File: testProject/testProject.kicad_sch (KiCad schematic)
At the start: 2 parts

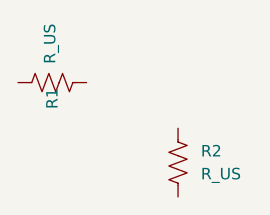
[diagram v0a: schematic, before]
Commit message: Fixed the symbol subsection error
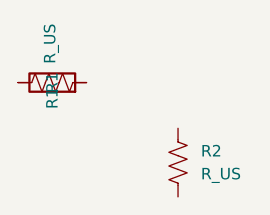
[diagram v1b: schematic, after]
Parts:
- added R1: (no value), symbol Device:R
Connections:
- net at R1.1: now also R1.1
- net at R1.2: now also R1.2
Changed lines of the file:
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@@
 	(generator_version "8.0")
 	(paper "A4")
-	(symbol
+(symbol
+        (lib_id "Device:R")
+        (at 146.05 53.34 90)
+        (unit 1)
+        (exclude_from_sim no)
+        (in_bom yes)
+        (on_board yes)
+        (dnp no)
+        (fields_autoplaced yes)
+        (property "Reference" "R1"
+            (at 146.05 53.34 0)
+            (effects
+                (font
+                    (size 1.27 1.27)
+                )
+            )
+        )
+        (property "Value" ""
+            (at 146.05 53.34 0)
+            (effects
+                (font
+                    (size 1.27 1.27)
+                )
+            )
+        )
+        (property "Footprint" ""
+            (at 146.05 53.34 0)
+            (effects
+                (font
+                    (size 1.27 1.27)
+                )
+                (hide yes)
+            )
+        )
+        (property "Datasheet" "~"
+            (at 146.05 53.34 0)
+            (effects
+                (font
+                    (size 1.27 1.27)
+                )
+                (hide yes)
+            )
+        )
+        (property "Description" "esistor"
+            (at 146.05 53.34 0)
+            (effects
+                (font
+                    (size 1.27 1.27)
+                )
+                (hide yes)
+            )
+        )
+        (instances
+            (project "temp_59526c9f-d2d4-4c47-ba25-9347dc717d36"
+                (path "/59526c9f-d2d4-4c47-ba25-9347dc717d36"
+                    (reference "R1")
+                    (unit 1)
+                )
+            )
+        )
+    )
+ 	(symbol
 		(lib_id "Device:R_US")
 		(at 146.05 53.34 90)

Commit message: The thing is buggy but it works
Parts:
- removed R1, R2: R_US, symbol Device:R_US
- removed R1: (no value), symbol Device:R
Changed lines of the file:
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@@
 	(generator_version "8.0")
 	(paper "A4")
-(symbol
-        (lib_id "Device:R")
-        (at 146.05 53.34 90)
-        (unit 1)
-        (exclude_from_sim no)
-        (in_bom yes)
-        (on_board yes)
-        (dnp no)
-        (fields_autoplaced yes)
-        (property "Reference" "R1"
-            (at 146.05 53.34 0)
-            (effects
-                (font
-                    (size 1.27 1.27)
-                )
-            )
-        )
-        (property "Value" ""
-            (at 146.05 53.34 0)
-            (effects
-                (font
-                    (size 1.27 1.27)
-                )
-            )
-        )
-        (property "Footprint" ""
-            (at 146.05 53.34 0)
-            (effects
-                (font
-                    (size 1.27 1.27)
-                )
-                (hide yes)
-            )
-        )
-        (property "Datasheet" "~"
-            (at 146.05 53.34 0)
-            (effects
-                (font
-                    (size 1.27 1.27)
-                )
-                (hide yes)
-            )
-        )
-        (property "Description" "esistor"
-            (at 146.05 53.34 0)
-            (effects
-                (font
-                    (size 1.27 1.27)
-                )
-                (hide yes)
-            )
-        )
-        (instances
-            (project "temp_59526c9f-d2d4-4c47-ba25-9347dc717d36"
-                (path "/59526c9f-d2d4-4c47-ba25-9347dc717d36"
-                    (reference "R1")
-                    (unit 1)
-                )
-            )
-        )
-    )
- 	(symbol
-		(lib_id "Device:R_US")
-		(at 146.05 53.34 90)
-		(unit 1)
-		(exclude_from_sim no)
-		(in_bom yes)
-		(on_board yes)
-		(dnp no)
-		(property "Reference" "R1"
-			(at 146.05 55.118 0)
-			(effects
-				(font
-					(size 1.27 1.27)
-				)
-			)
-		)
-		(property "Value" "R_US"
-			(at 145.796 49.022 0)
-			(effects
-				(font
-					(size 1.27 1.27)
-				)
-			)
-		)
-		(property "Footprint" ""
-			(at 146.05 53.34 0)
-			(effects
-				(font
-					(size 1.27 1.27)
-				)
-				(hide yes)
-			)
-		)
-		(property "Datasheet" "~"
-			(at 146.05 53.34 0)
-			(effects
-				(font
-					(size 1.27 1.27)
-				)
-				(hide yes)
-			)
-		)
-		(property "Description" "esistor, US symbol"
-			(at 146.05 53.34 0)
-			(effects
-				(font
-					(size 1.27 1.27)
-				)
-				(hide yes)
-			)
-		)
-		(pin "2"
-		)
-		(pin "1"
-		)
-		(instances
-			(project "testProject"
-				(path "/59526c9f-d2d4-4c47-ba25-9347dc717d36"
-					(reference "R1")
-					(unit 1)
-				)
-			)
-		)
-	)
-	(symbol
-		(lib_id "Device:R_US")
-		(at 160.02 62.23 0)
-		(unit 1)
-		(exclude_from_sim no)
-		(in_bom yes)
-		(on_board yes)
-		(dnp no)
-		(fields_autoplaced yes)
-		(property "Reference" "R2"
-			(at 162.56 60.9599 0)
-			(effects
-				(font
-					(size 1.27 1.27)
-				)
-				(justify left)
-			)
-		)
-		(property "Value" "R_US"
-			(at 162.56 63.4999 0)
-			(effects
-				(font
-					(size 1.27 1.27)
-				)
-				(justify left)
-			)
-		)
-		(property "Footprint" ""
-			(at 161.036 62.484 90)
-			(effects
-				(font
-					(size 1.27 1.27)
-				)
-				(hide yes)
-			)
-		)
-		(property "Datasheet" "~"
-			(at 160.02 62.23 0)
-			(effects
-				(font
-					(size 1.27 1.27)
-				)
-				(hide yes)
-			)
-		)
-		(property "Description" "Resistor, US symbol"
-			(at 160.02 62.23 0)
-			(effects
-				(font
-					(size 1.27 1.27)
-				)
-				(hide yes)
-			)
-		)
-		(pin "2"
-		)
-		(pin "1"
-		)
-		(instances
-			(project "testProject"
-				(path "/59526c9f-d2d4-4c47-ba25-9347dc717d36"
-					(reference "R2")
-					(unit 1)
-				)
-			)
-		)
-	)
 	(sheet_instances
 		(path "/"

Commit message: cleaned up notebook
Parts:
- added C1, C2: C, symbol Device:C
- added R1: R, symbol Device:R
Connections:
- new net: C2.1, R1.1
- new net: C1.1, C2.2
- new net: C1.2, R1.2

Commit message: changed config.yaml
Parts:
- removed C1, C2: C, symbol Device:C
- removed R1: R, symbol Device:R

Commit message: Added add_wires in GUI
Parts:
- added BAT1: attery, symbol Device:Battery
- added LED1: ED, symbol Device:LED
- added R1: (no value), symbol Device:R
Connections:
- new net: BAT1.1 (+), R1.2
- new net: BAT1.2 (-), LED1.1 (K), LED1.2 (A), R1.1

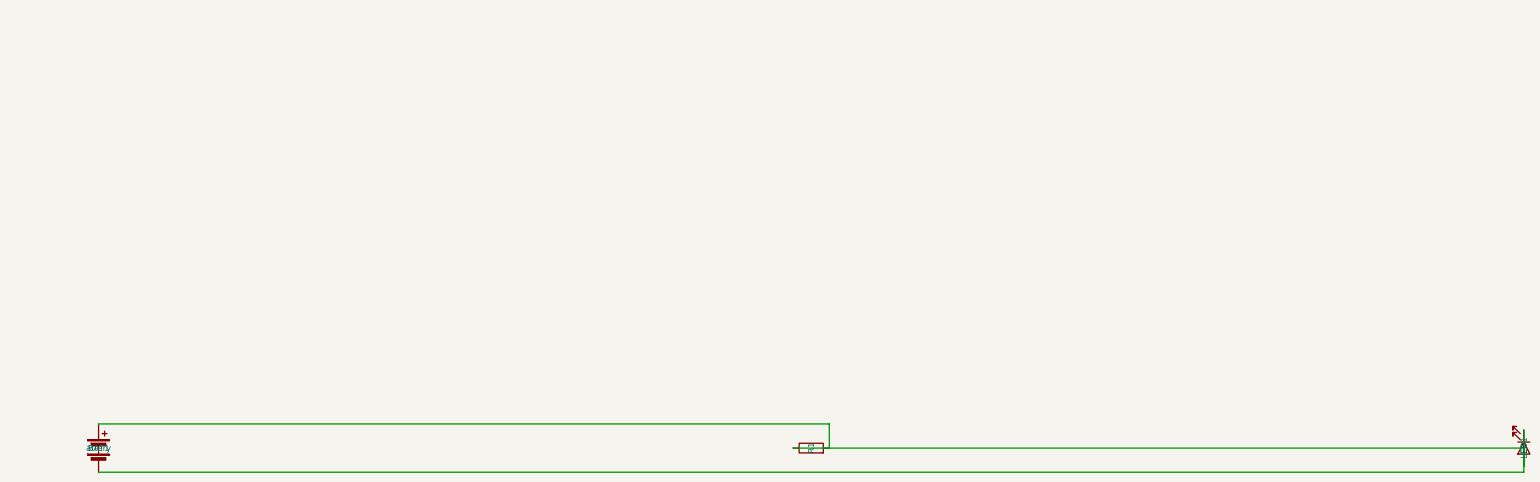
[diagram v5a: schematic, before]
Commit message: still needs error handling for wire functions
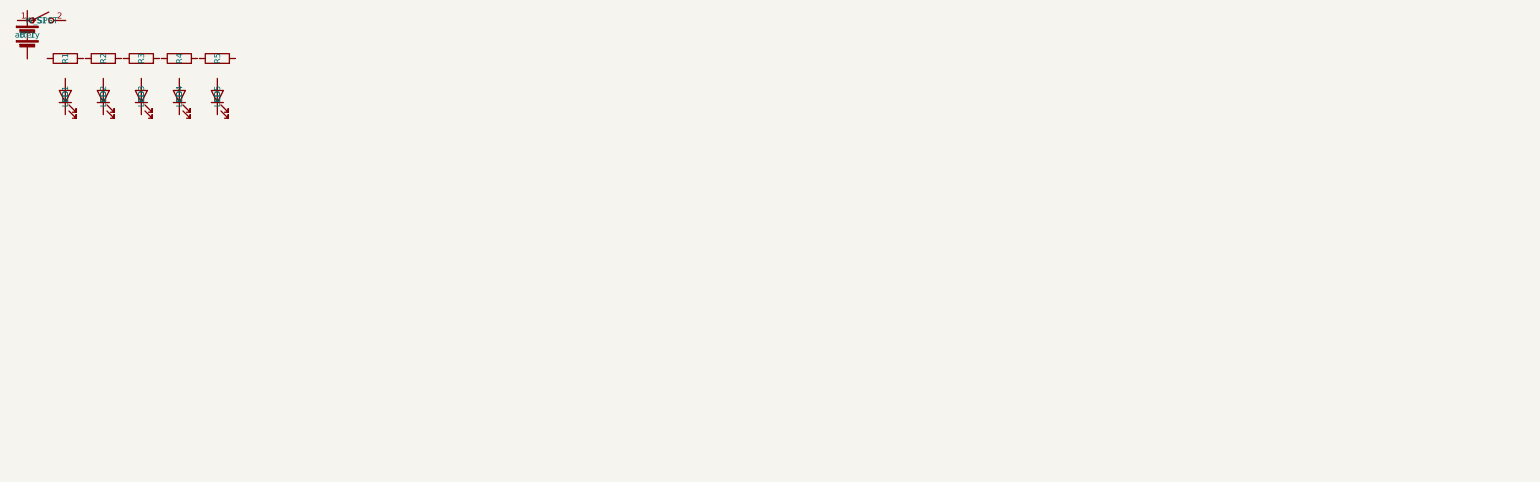
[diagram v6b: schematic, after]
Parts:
- removed BAT1: attery, symbol Device:Battery
- added BT1: attery, symbol Device:Battery
- added LED2, LED3, LED4, LED5: ED, symbol Device:LED
- added R2, R3, R4, R5: (no value), symbol Device:R
- added S1: W_SPST, symbol Switch:SW_SPST
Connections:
- now unconnected: LED1.1 (K), LED1.2 (A), R1.1

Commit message: exit
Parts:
- removed LED1, LED2, LED3, LED4, LED5: ED, symbol Device:LED
- removed R2, R3, R4, R5: (no value), symbol Device:R
- removed S1: W_SPST, symbol Switch:SW_SPST
- added C1: (no value), symbol Device:C
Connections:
- net at BT1.1 (+): now also R1.1
- net at BT1.2 (-): now also C1.2
- net at R1.2: now also C1.1

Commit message: removed unneccessary files, clean up notebook
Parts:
- removed BT1: attery, symbol Device:Battery
- removed C1: (no value), symbol Device:C
- removed R1: (no value), symbol Device:R
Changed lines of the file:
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@@
 	(generator_version "8.0")
 	(paper "A4")
- (wire
-		(pts
-			(xy 42 14.92) (xy 42 16.19)
-		)
-		(stroke
-			(width 0)
-			(type default)
-		)
-	)
- (wire
-		(pts
-			(xy 20 14.92) (xy 42 14.92)
-		)
-		(stroke
-			(width 0)
-			(type default)
-		)
-	)
- (wire
-		(pts
-			(xy 42 23.81) (xy 42 28.19)
-		)
-		(stroke
-			(width 0)
-			(type default)
-		)
-	)
- (wire
-		(pts
-			(xy 20 35.81) (xy 20 25.08)
-		)
-		(stroke
-			(width 0)
-			(type default)
-		)
-	)
- (wire
-		(pts
-			(xy 42 35.81) (xy 20 35.81)
-		)
-		(stroke
-			(width 0)
-			(type default)
-		)
-	)
-(symbol
-        (lib_id "Device:C")
-        (at 42 32 0)
-        (unit 1)
-        (exclude_from_sim no)
-        (in_bom yes)
-        (on_board yes)
-        (dnp no)
-        (fields_autoplaced yes)
-        (property "Reference" "C1"
-            (at 42 32 0)
-            (effects
-                (font
-                    (size 1.27 1.27)
-                )
-            )
-        )
-        (property "Value" ""
-            (at 42 32 0)
-            (effects
-                (font
-                    (size 1.27 1.27)
-                )
-            )
-        )
-        (property "Footprint" ""
-            (at 42 32 0)
-            (effects
-                (font
-                    (size 1.27 1.27)
-                )
-                (hide yes)
-            )
-        )
-        (property "Datasheet" "~"
-            (at 42 32 0)
-            (effects
-                (font
-                    (size 1.27 1.27)
-                )
-                (hide yes)
-            )
-        )
-        (property "Description" "npolarized capacitor"
-            (at 42 32 0)
-            (effects
-                (font
-                    (size 1.27 1.27)
-                )
-                (hide yes)
-            )
-        )
-        (pin "1")
-        (pin "2")
-        (instances
-            (project "temp_dea647a7-e0d8-45e4-9bce-23c7e387cf2b"
-                (path "/dea647a7-e0d8-45e4-9bce-23c7e387cf2b"
-                    (reference "C1")
-                    (unit 1)
-                )
-            )
-        )
-    )
-(symbol
-        (lib_id "Device:R")
-        (at 42 20 0)
-        (unit 1)
-        (exclude_from_sim no)
-        (in_bom yes)
-        (on_board yes)
-        (dnp no)
-        (fields_autoplaced yes)
-        (property "Reference" "R1"
-            (at 42 20 0)
-            (effects
-                (font
-                    (size 1.27 1.27)
-                )
-            )
-        )
-        (property "Value" ""
-            (at 42 20 0)
-            (effects
-                (font
-                    (size 1.27 1.27)
-                )
-            )
-        )
-        (property "Footprint" ""
-            (at 42 20 0)
-            (effects
-                (font
-                    (size 1.27 1.27)
-                )
-                (hide yes)
-            )
-        )
-        (property "Datasheet" "~"
-            (at 42 20 0)
-            (effects
-                (font
-                    (size 1.27 1.27)
-                )
-                (hide yes)
-            )
-        )
-        (property "Description" "esistor"
-            (at 42 20 0)
-            (effects
-                (font
-                    (size 1.27 1.27)
-                )
-                (hide yes)
-            )
-        )
-        (pin "1")
-        (pin "2")
-        (instances
-            (project "temp_dea647a7-e0d8-45e4-9bce-23c7e387cf2b"
-                (path "/dea647a7-e0d8-45e4-9bce-23c7e387cf2b"
-                    (reference "R1")
-                    (unit 1)
-                )
-            )
-        )
-    )
-(symbol
-        (lib_id "Device:Battery")
-        (at 20 20 0)
-        (unit 1)
-        (exclude_from_sim no)
-        (in_bom yes)
-        (on_board yes)
-        (dnp no)
-        (fields_autoplaced yes)
-        (property "Reference" "BT1"
-            (at 20 20 0)
-            (effects
-                (font
-                    (size 1.27 1.27)
-                )
-            )
-        )
-        (property "Value" "attery"
-            (at 20 20 0)
-            (effects
-                (font
-                    (size 1.27 1.27)
-                )
-            )
-        )
-        (property "Footprint" ""
-            (at 20 20 0)
-            (effects
-                (font
-                    (size 1.27 1.27)
-                )
-                (hide yes)
-            )
-        )
-        (property "Datasheet" "~"
-            (at 20 20 0)
-            (effects
-                (font
-                    (size 1.27 1.27)
-                )
-                (hide yes)
-            )
-        )
-        (property "Description" "ultiple-cell battery"
-            (at 20 20 0)
-            (effects
-                (font
-                    (size 1.27 1.27)
-                )
-                (hide yes)
-            )
-        )
-        (pin "1")
-        (pin "2")
-        (instances
-            (project "temp_dea647a7-e0d8-45e4-9bce-23c7e387cf2b"
-                (path "/dea647a7-e0d8-45e4-9bce-23c7e387cf2b"
-                    (reference "BT1")
-                    (unit 1)
-                )
-            )
-        )
-    )
- 	(sheet_instances
+	(sheet_instances
 		(path "/"
 			(page "1")
